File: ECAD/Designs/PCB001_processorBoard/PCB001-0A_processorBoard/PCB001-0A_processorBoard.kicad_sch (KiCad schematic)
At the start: 0 parts

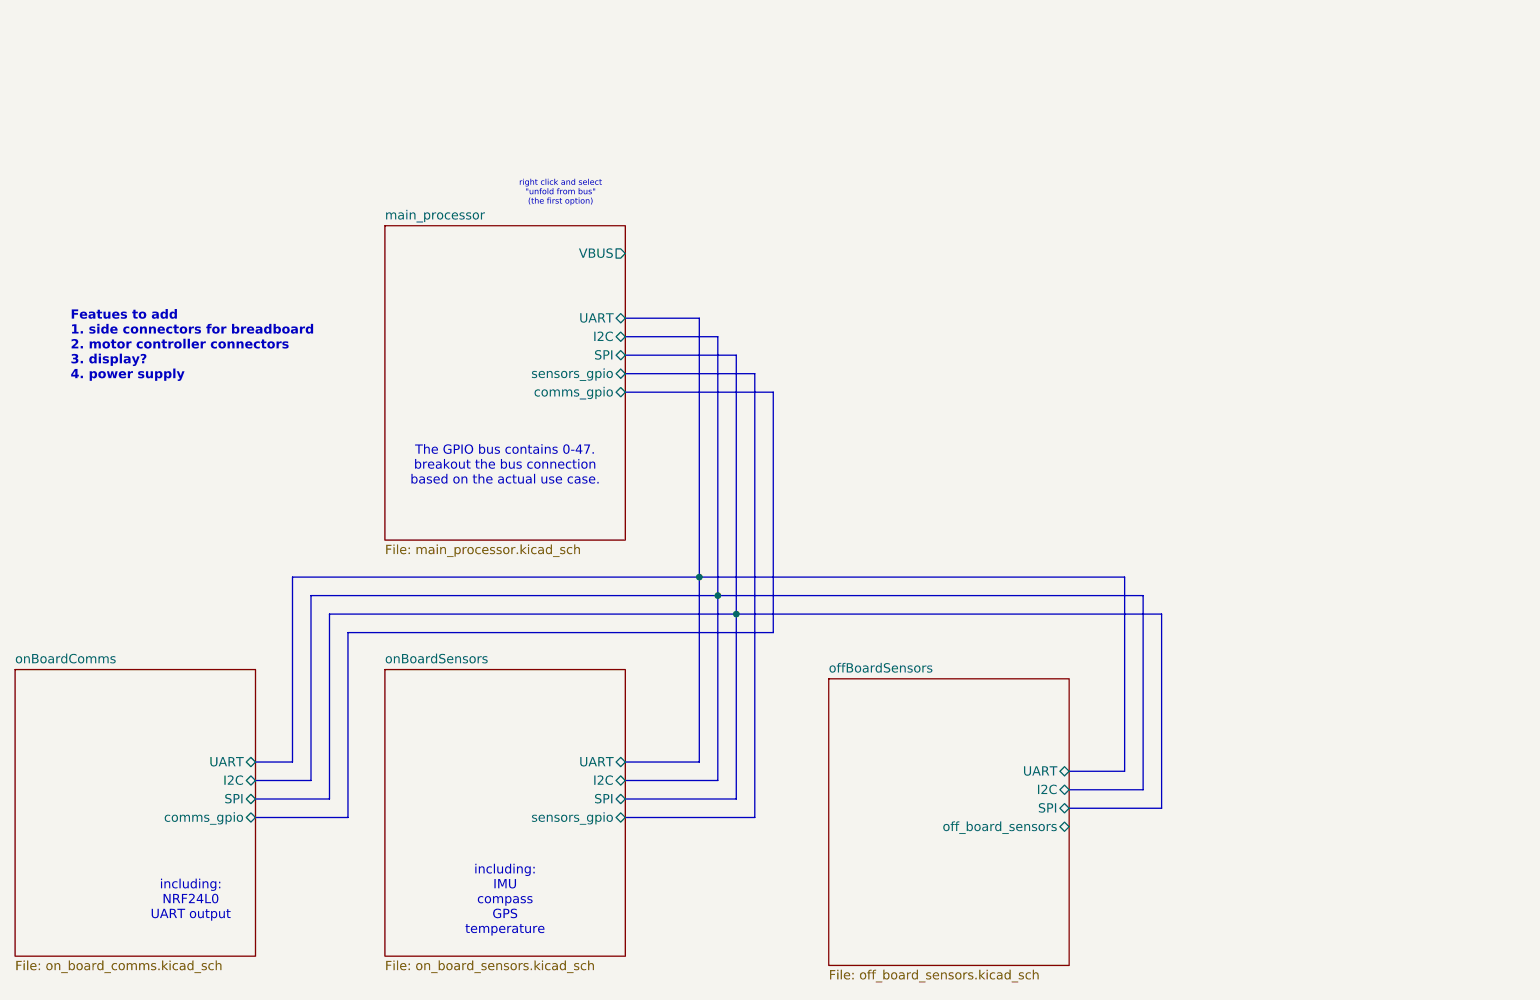
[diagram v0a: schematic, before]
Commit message: added more connectors to the side of the PCB, added a basic power supply, and began putting parts on the PCB.
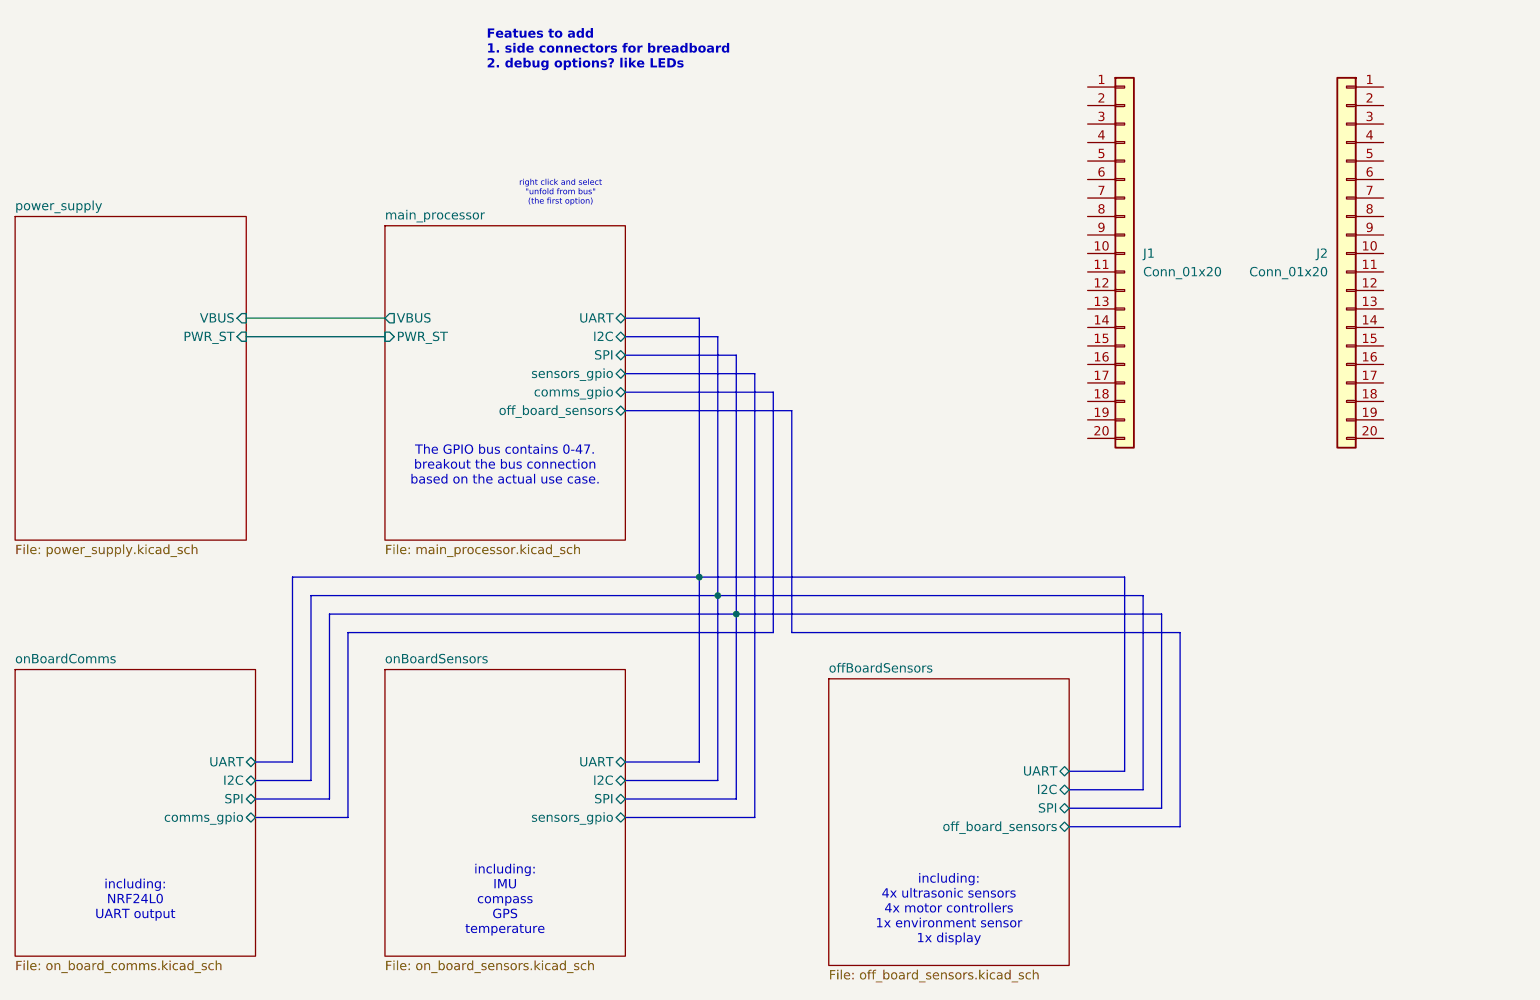
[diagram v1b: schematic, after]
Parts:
- added J1, J2: Conn_01x20, Connector_PinHeader_2.54mm:PinHeader_1x20_P2.54mm_Vertical, symbol Connector_Generic:Conn_01x20
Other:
- added sheet power_supply (power_supply.kicad_sch)
- sheet main_processor ports: added PWR_ST, off_board_sensors; removed none
- note added: "Featues to add 1. side connectors for breadboard 2. debug options? like LEDs"
- note added: "including: 4x ultrasonic sensors 4x motor controllers 1x environment sensor 1x display"
- note removed: "Featues to add 1. side connectors for breadboard 2. motor controller connectors 3. display? 4. power supply"

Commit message: updated schematics
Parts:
- added H1, H2, H3, H4: M2, MountingHole:MountingHole_2.2mm_M2, symbol Mechanical:MountingHole
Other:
- sheet power_supply ports: added 5V IN; removed none
- note added: "putting these here so that we can get a sense of scale with the PCB"
- note added: "the pcb MUST include atleast 3 mounting holes, but 4 would be better."
- moved on the sheet: J2
